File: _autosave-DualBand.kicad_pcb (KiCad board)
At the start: 2 copper layers, 99.6 x 50.2 mm, 66 parts, among them J1 Conn_01x03_Male, J2 Conn_01x03_Male, J3 Conn_01x10_Male, J4 Conn_01x03_Male, J5 Conn_01x02_Male, J6 Conn_01x10_Male, J7 Conn_01x01_Male, P1 AD8402ARUZ1, SW1 SW_Push, U1 LD1117V33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

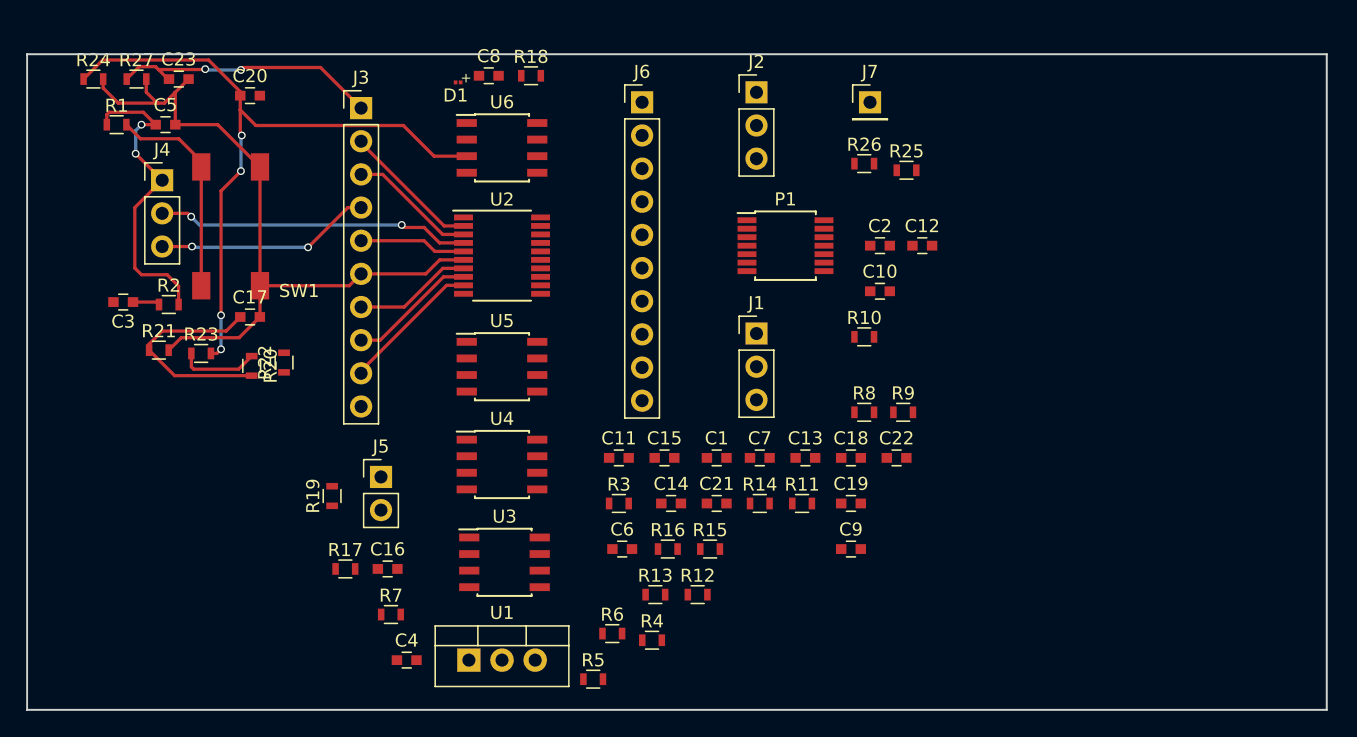
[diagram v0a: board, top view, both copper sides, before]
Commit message: Recreates PCB based on new layout
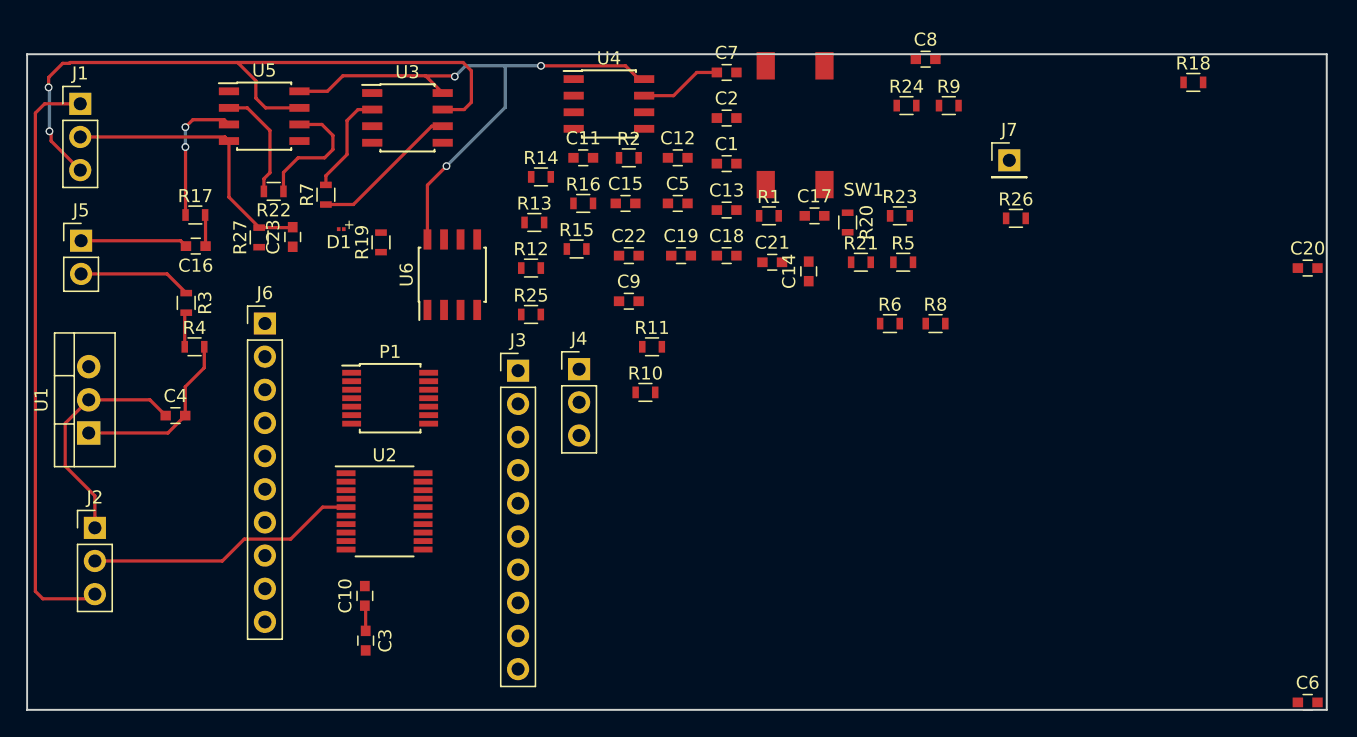
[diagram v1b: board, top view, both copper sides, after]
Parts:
- moved C20 82.1 mm to (210.5, 109.5)
- moved R24 62.3 mm to (179.8, 97.0)
- moved J2 60.7 mm to (117.6, 129.4)
- moved J1 54.7 mm to (116.5, 96.9)
- moved R23 54.6 mm to (179.3, 105.5)
- moved R21 54.2 mm to (176.3, 109.0)
- moved C6 53.8 mm to (210.5, 142.7)
- moved R18 50.7 mm to (201.7, 95.2)
- moved R1 50.5 mm to (169.2, 105.5)
- moved R20 47.0 mm to (175.3, 106.0)
- moved C10 45.8 mm to (138.3, 134.6), turned to 90 degrees
- moved C17 43.9 mm to (172.7, 105.5)
- moved SW1 43.9 mm to (173.5, 94.0)
- moved R4 41.6 mm to (125.2, 115.5)
- moved R5 39.8 mm to (179.5, 109.0)
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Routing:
- net Net-(C20-Pad1): track 53.8 -> 0.00 mm, vias 4 -> 0
- net +9V: track 6.14 -> 59.3 mm, vias 0 -> 2
- net /~SD: track 0.00 -> 45.3 mm, vias 0 -> 3
- net +3V3: track 0.00 -> 45.3 mm
- net Net-(C5-Pad1): track 24.3 -> 0.00 mm, vias 2 -> 0
- net Net-(J4-Pad2): track 24.0 -> 0.00 mm, vias 2 -> 0
- net GND: track 57.1 -> 35.5 mm
- net Net-(C23-Pad1): track 21.0 -> 0.00 mm, vias 2 -> 0
- net Net-(C4-Pad1): track 0.00 -> 17.9 mm
- net Net-(C17-Pad1): track 17.0 -> 0.00 mm
- net Net-(J3-Pad4): track 16.5 -> 0.00 mm, vias 2 -> 0
- net Net-(R1-Pad2): track 16.4 -> 0.00 mm
- net /DVCC: track 10.3 -> 22.9 mm
- net Net-(C8-Pad2): track 0.00 -> 11.4 mm
- net Net-(J3-Pad9): track 10.7 -> 0.00 mm
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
